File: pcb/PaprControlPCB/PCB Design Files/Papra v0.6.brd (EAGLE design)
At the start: 36 x 45 mm, 40 parts, among them Q1 AO3400A (C20917), Q2 AO3400A (C20917), U1 LP2985-50DBVR (C74511), U2 ATTINYX04SOIC14

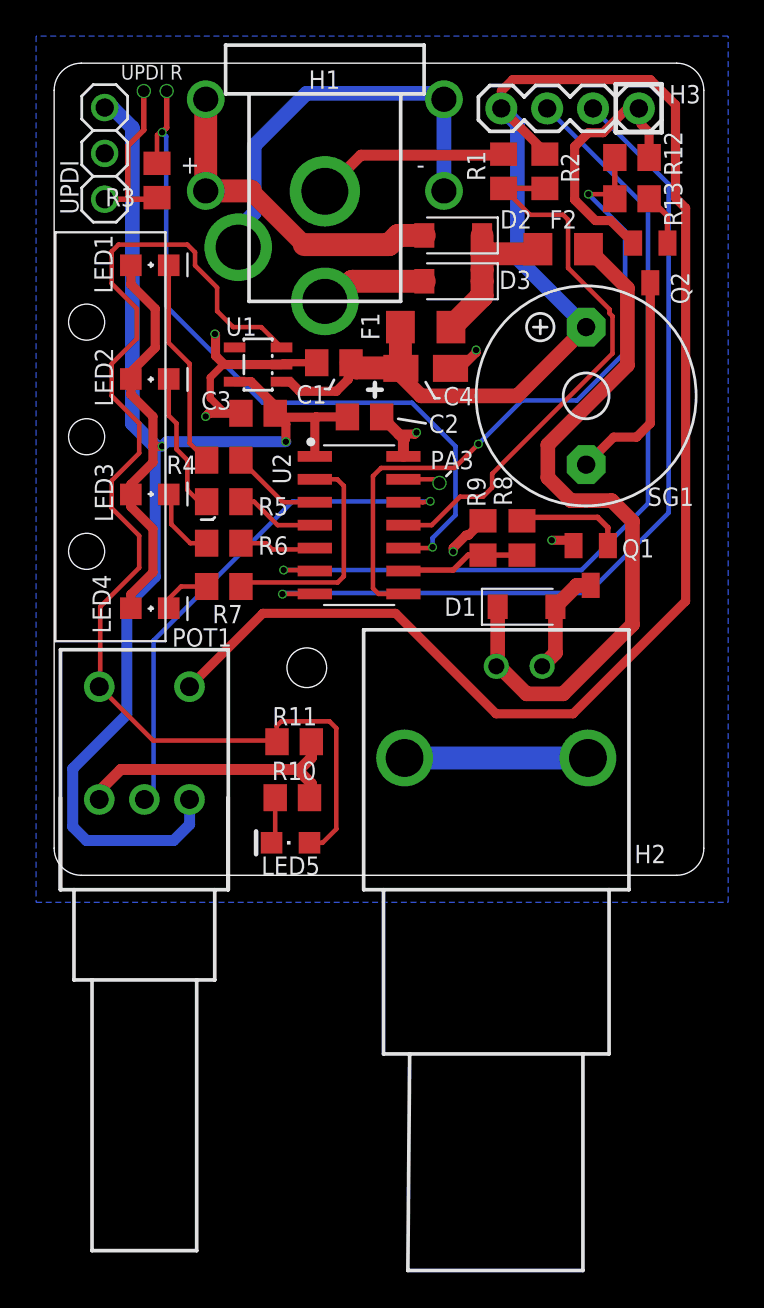
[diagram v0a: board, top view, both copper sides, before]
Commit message: Board ready for review
Closes #53
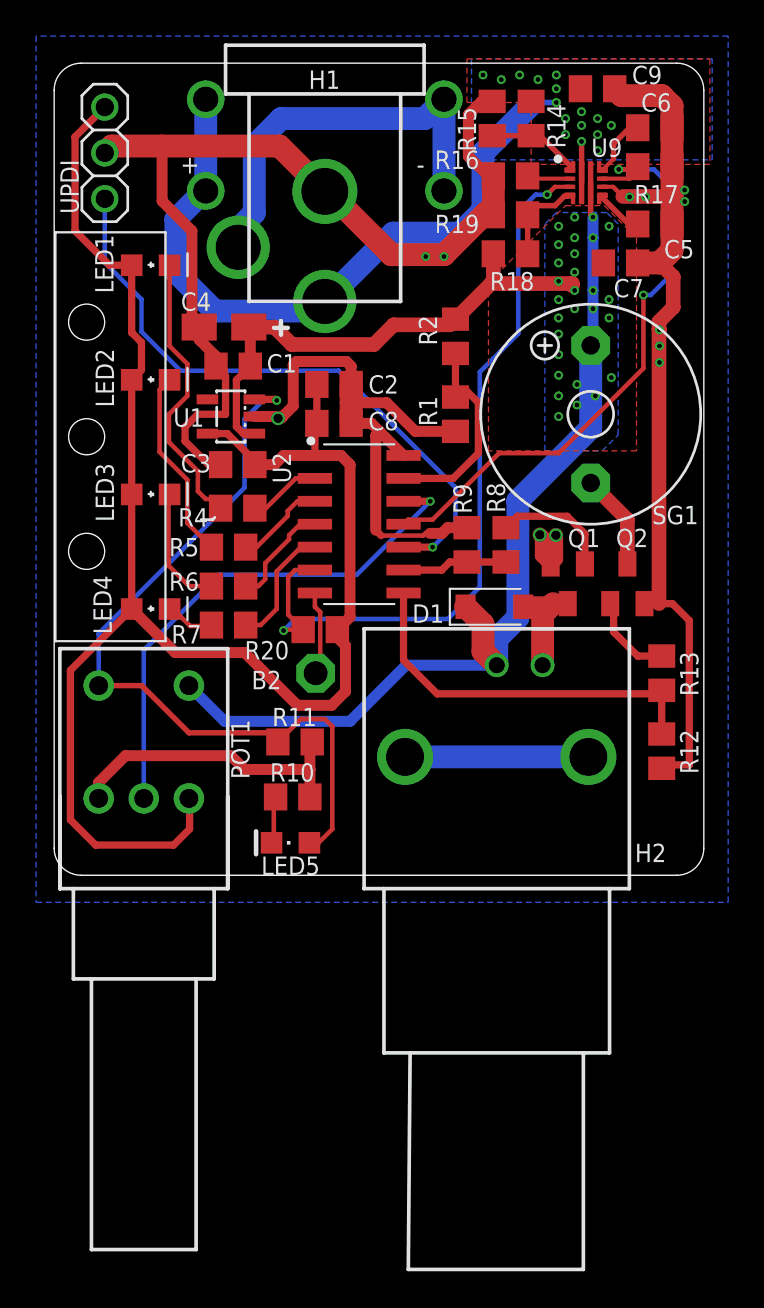
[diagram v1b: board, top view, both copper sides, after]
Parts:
- removed D2, D3: MBR2H100SFT3G C96515, Diode:SODFL3718X115
- removed F1, F2: 13.2V 1.8A (C70081), SparkFun-Fuses:1206
- removed H3: 1X4-BIG, adafruit:1X04-BIG
- removed R3: 1K2 0805W8F1201T5E (C17379), rcl:R0805
- added B2: PTR1PAD1-13, testpad:P1-13
- added C5: 3.6nF, rcl:C0805
- added C6: 2.7nF, rcl:C0805
- added C7, C8: 1uF CL21B105KBFNNNE (C28323), rcl:C0805
- added C9: .1uF CL21B104KBFNNNE (C49678 ), rcl:C0805
- added R14: 470K, rcl:R0805
- added R15: 82K, rcl:R0805
- added R16: 390K, rcl:R0805
- added R17: 1K, rcl:R0805
- added R18: 360K, rcl:R0805
- added R19: 56K, rcl:R0805
- added R20: 10K 0805W8F1002T5E (C17414), rcl:R0805
- added U9: TPS259472ARPWR, TI e-Fuse:QFN45P200X200X100-16N
- LED1, LED2, LED3, LED4: value NCD0805G1 C84260 -> NCD0603G1 C84267
- Q1, Q2: value AO3400A (C20917) -> BSS123
- moved R12 32.9 mm to (18.7, -15.6), turned to 90 degrees
- moved R13 26.3 mm to (18.7, -11.3), turned to 270 degrees
- moved Q2 17.8 mm to (16.8, -6.35), turned to 0 degrees
- moved R1 13.7 mm to (7.24, 3.05), turned to 90 degrees
- moved C4 11.4 mm to (-5.59, 7.87), turned to 0 degrees
- moved R2 10.4 mm to (7.24, 7.37)
- moved C1 5.58 mm to (-5.08, 5.71)
- moved U1 3.25 mm to (-5.21, 2.92)
- moved C3 3.06 mm to (-4.83, 0.25)
- moved R4 2.77 mm to (-4.83, -2.16)
- moved R5 2.53 mm to (-5.33, -4.32)
- moved C2 2.47 mm to (0.51, 4.70)
- moved R6 2.39 mm to (-5.33, -6.48)
- moved R7 2.15 mm to (-5.33, -8.64)
- moved D1 1.78 mm to (9.40, -7.62)
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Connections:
- removed net 12V-BAT: BATT+.1, BATT+.2, D2.2
- removed net 12V-DC: D3.2, H1.PWR
- removed net 12V-DIODEOR: D2.1, D3.1, F1.1, F2.1
- removed net 12V-FAN: D1.1, F2.2, H2.SIGNAL
- removed net EXPANSIONRX: H3.3, U2.6
- removed net EXPANSIONTX: H3.2, U2.7
- removed net UNUSED: U2.13
- removed net UPDI/RST: R3.1, U2.10
- new net 12V-IN: BATT+.1, BATT+.2, C9.1, H1.PWR, R14.2, U9.5
- new net DEBUGTX: B2.TP, U2.7
- new net DVDT: C5.1, U9.7
- new net EN/UVLO: R14.1, R15.2, U9.1
- new net ILM: R17.2, U2.11, U9.9
- new net ITIMER: C6.1, U9.10
- new net OVCSEL: R16.2, U9.2
- new net PG: R20.1, U2.6, U9.3
- new net PGTH: R18.1, R19.2, U9.4
- net +12V: now also C7.1, D1.1, H2.SIGNAL, R18.2, U9.6; no longer F1.2, H3.4
- net +5V: now also C8.1, R20.2
- net ADC-BAT: now also U2.13; no longer U2.11
- net GND: now also C5.2, C6.2, C7.2, C8.2, C9.2, R15.1, R16.1, R17.1, R19.1, U9.8; no longer H3.1
- net LED1: now also U2.2; no longer U2.3
- net LED2: now also U2.3; no longer U2.4
- net LED3: now also U2.4; no longer U2.5
- net LED4: now also U2.5; no longer U2.2
- net UPDI: now also U2.10; no longer R3.2
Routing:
- net GND: track 67.1 -> 158.2 mm, vias 6 -> 12
- net EXPANSIONTX: track 49.2 -> 0.00 mm, vias 1 -> 0
- net EXPANSIONRX: track 47.7 -> 0.00 mm, vias 1 -> 0
- net PG: track 0.00 -> 43.0 mm, vias 0 -> 2
- net 12V-IN: track 0.00 -> 41.5 mm, vias 0 -> 16
- net UPDI/RST: track 41.0 -> 0.00 mm, vias 3 -> 0
- net 12V-FAN: track 39.8 -> 0.00 mm
- net ILM: track 0.00 -> 34.4 mm, vias 0 -> 2
- net +12V: track 113.9 -> 80.7 mm, vias 0 -> 28
- net UPDI: track 9.30 -> 34.6 mm
- net PWRON: track 64.1 -> 43.8 mm, vias 0 -> 1
- net ADC-BAT: track 31.0 -> 11.5 mm
- net 12V-BAT: track 18.6 -> 0.00 mm
- net BUZZER: track 38.3 -> 21.3 mm, vias 2 -> 0
- net 12V-DIODEOR: track 9.00 -> 0.00 mm
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- added copper zone on layer 1, net +12V
- added copper zone on layer 16, net +12V
- added copper zone on layer 1, net 12V-IN
- added copper zone on layer 16, net 12V-IN
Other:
- board text added: "27JULY2021"
- board text added: "PAPRA V0.6"
- board text added: "TETRABIO.ORG"
- board text removed: "2021 TETRABIO.ORG"
- board text removed: "26APR2021"
- board text removed: "PA3"
- board text removed: "PAPRA V0.5"
- board text removed: "UPDI R"

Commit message: Updates based on feedback
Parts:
- R15: value 82K -> 75K
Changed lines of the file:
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@@
 <grid distance="1" unitdist="mil" unit="mil" style="lines" multiple="1" display="yes" altdistance="5" altunitdist="mil" altunit="mil"/>
 <layers>
-<layer number="1" name="Top" color="4" fill="1" visible="no" active="yes"/>
+<layer number="1" name="Top" color="4" fill="1" visible="yes" active="yes"/>
 <layer number="2" name="Route2" color="16" fill="1" visible="no" active="no"/>
 <layer number="3" name="Route3" color="17" fill="1" visible="no" active="no"/>
@@
 <layer number="14" name="Route14" color="22" fill="1" visible="no" active="no"/>
 <layer number="15" name="Route15" color="23" fill="1" visible="no" active="no"/>
-<layer number="16" name="Bottom" color="1" fill="1" visible="yes" active="yes"/>
+<layer number="16" name="Bottom" color="1" fill="1" visible="no" active="yes"/>
 <layer number="17" name="Pads" color="2" fill="1" visible="yes" active="yes"/>
 <layer number="18" name="Vias" color="2" fill="1" visible="yes" active="yes"/>
 <layer number="19" name="Unrouted" color="6" fill="1" visible="yes" active="yes"/>
 <layer number="20" name="Dimension" color="24" fill="1" visible="yes" active="yes"/>
-<layer number="21" name="tPlace" color="7" fill="1" visible="no" active="yes"/>
+<layer number="21" name="tPlace" color="7" fill="1" visible="yes" active="yes"/>
 <layer number="22" name="bPlace" color="7" fill="1" visible="no" active="yes"/>
-<layer number="23" name="tOrigins" color="15" fill="1" visible="no" active="yes"/>
+<layer number="23" name="tOrigins" color="15" fill="1" visible="yes" active="yes"/>
 <layer number="24" name="bOrigins" color="15" fill="1" visible="no" active="yes"/>
-<layer number="25" name="tNames" color="7" fill="1" visible="no" active="yes"/>
+<layer number="25" name="tNames" color="7" fill="1" visible="yes" active="yes"/>
 <layer number="26" name="bNames" color="7" fill="1" visible="no" active="yes"/>
 <layer number="27" name="tValues" color="7" fill="1" visible="no" active="yes"/>
@@
 <layer number="37" name="tTest" color="7" fill="1" visible="no" active="yes"/>
 <layer number="38" name="bTest" color="7" fill="1" visible="no" active="yes"/>
-<layer number="39" name="tKeepout" color="4" fill="11" visible="no" active="yes"/>
+<layer number="39" name="tKeepout" color="4" fill="11" visible="yes" active="yes"/>
 <layer number="40" name="bKeepout" color="1" fill="11" visible="no" active="yes"/>
-<layer number="41" name="tRestrict" color="4" fill="10" visible="no" active="yes"/>
+<layer number="41" name="tRestrict" color="4" fill="10" visible="yes" active="yes"/>
 <layer number="42" name="bRestrict" color="1" fill="10" visible="no" active="yes"/>
 <layer number="43" name="vRestrict" color="2" fill="10" visible="no" active="yes"/>
@@
 <layer number="49" name="Reference" color="7" fill="1" visible="no" active="yes"/>
 <layer number="50" name="dxf" color="3" fill="1" visible="no" active="no"/>
-<layer number="51" name="tDocu" color="7" fill="1" visible="no" active="yes"/>
+<layer number="51" name="tDocu" color="7" fill="1" visible="yes" active="yes"/>
 <layer number="52" name="bDocu" color="7" fill="1" visible="no" active="yes"/>
 <layer number="53" name="tGND_GNDA" color="7" fill="9" visible="no" active="no"/>
@@
 </layers>
 <board>
-<fusionsync huburn="a.YnVzaW5lc3M6ZmFjdG9yeW9wdGlj" projecturn="a.YnVzaW5lc3M6ZmFjdG9yeW9wdGljI0QyMDIxMDYwOTQxOTQ3NjY1Ng" f3durn="urn:adsk.wipprod:dm.lineage:61lF-rPKTo2oqacU3GTP8Q" pcbguid="" lastpulledtime="" lastsyncedchangeguid="" latestrevisionid="e0e9a423-17c1-4b6c-8c41-111679188c98" lastsyncedrevisionid="e0e9a423-17c1-4b6c-8c41-111679188c98" lastboardhashguid="b5a4f31a-817b-64f9-f622-9de04c436f70" lastpushedtime="2021-07-27T13:45:13Z" linktopcb3d="true"/>
+<fusionsync huburn="a.YnVzaW5lc3M6ZmFjdG9yeW9wdGlj" projecturn="a.YnVzaW5lc3M6ZmFjdG9yeW9wdGljI0QyMDIxMDYwOTQxOTQ3NjY1Ng" f3durn="urn:adsk.wipprod:dm.lineage:61lF-rPKTo2oqacU3GTP8Q" pcbguid="" lastpulledtime="" lastsyncedchangeguid="" latestrevisionid="e0e9a423-17c1-4b6c-8c41-111679188c98" lastsyncedrevisionid="e0e9a423-17c1-4b6c-8c41-111679188c98" lastboardhashguid="b5a4f31a-817b-64f9-f622-9de04c436f70" lastpushedtime="2021-07-27T13:45:13Z" linktopcb3d="false"/>
 <plain>
 <wire x1="19.5" y1="22.5" x2="-13.5" y2="22.5" width="0.001" layer="20"/>
@@
 <attribute name="VALUE" x="13.97" y="18.796" size="1.27" layer="27" rot="R90"/>
 </element>
-<element name="R15" library="rcl" library_urn="urn:adsk.eagle:library:334" package="R0805" package3d_urn="urn:adsk.eagle:package:23553/2" value="82K" x="9.271" y="19.431" smashed="yes" rot="R270">
+<element name="R15" library="rcl" library_urn="urn:adsk.eagle:library:334" package="R0805" package3d_urn="urn:adsk.eagle:package:23553/2" value="75K" x="9.271" y="19.431" smashed="yes" rot="R270">
 <attribute name="NAME" x="7.366" y="20.066" size="1.016" layer="25" font="vector" ratio="12" rot="R270"/>
 <attribute name="POPULARITY" value="85" x="9.271" y="19.431" size="1.778" layer="27" rot="R270" display="off"/>
